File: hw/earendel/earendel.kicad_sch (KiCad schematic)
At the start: 0 parts

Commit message: Add LED ring drivers
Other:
- added sheet Inner Ring (inner_ring.kicad_sch)
- added sheet MCU (mcu.kicad_sch)
- added sheet Outer Ring (outer_ring.kicad_sch)
- added sheet Power (power.kicad_sch)
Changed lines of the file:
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@@
 		(company "Aaron & Ryan Shappell")
+	)
+	(sheet
+		(at 132.08 109.22)
+		(size 26.67 13.97)
+		(fields_autoplaced yes)
+		(stroke
+			(width 0.1524)
+			(type solid)
+		)
+		(fill
+			(color 0 0 0 0.0000)
+		)
+		(property "Sheetname" "Outer Ring"
+			(at 132.08 108.5084 0)
+			(effects
+				(font
+					(size 1.27 1.27)
+				)
+				(justify left bottom)
+			)
+		)
+		(property "Sheetfile" "outer_ring.kicad_sch"
+			(at 132.08 123.7746 0)
+			(effects
+				(font
+					(size 1.27 1.27)
+				)
+				(justify left top)
+			)
+		)
+		(instances
+			(project "earendel"
+				(path "/9f298bf9-d1b7-4300-ae61-070881d679f0"
+					(page "5")
+				)
+			)
+		)
+	)
+	(sheet
+		(at 81.28 58.42)
+		(size 20.32 16.51)
+		(fields_autoplaced yes)
+		(stroke
+			(width 0.1524)
+			(type solid)
+		)
+		(fill
+			(color 0 0 0 0.0000)
+		)
+		(property "Sheetname" "MCU"
+			(at 81.28 57.7084 0)
+			(effects
+				(font
+					(size 1.27 1.27)
+				)
+				(justify left bottom)
+			)
+		)
+		(property "Sheetfile" "mcu.kicad_sch"
+			(at 81.28 75.5146 0)
+			(effects
+				(font
+					(size 1.27 1.27)
+				)
+				(justify left top)
+			)
+		)
+		(instances
+			(project "earendel"
+				(path "/9f298bf9-d1b7-4300-ae61-070881d679f0"
+					(page "2")
+				)
+			)
+		)
+	)
+	(sheet
+		(at 78.74 110.49)
+		(size 25.4 13.97)
+		(fields_autoplaced yes)
+		(stroke
+			(width 0.1524)
+			(type solid)
+		)
+		(fill
+			(color 0 0 0 0.0000)
+		)
+		(property "Sheetname" "Inner Ring"
+			(at 78.74 109.7784 0)
+			(effects
+				(font
+					(size 1.27 1.27)
+				)
+				(justify left bottom)
+			)
+		)
+		(property "Sheetfile" "inner_ring.kicad_sch"
+			(at 78.74 125.0446 0)
+			(effects
+				(font
+					(size 1.27 1.27)
+				)
+				(justify left top)
+			)
+		)
+		(instances
+			(project "earendel"
+				(path "/9f298bf9-d1b7-4300-ae61-070881d679f0"
+					(page "4")
+				)
+			)
+		)
+	)
+	(sheet
+		(at 129.54 58.42)
+		(size 25.4 15.24)
+		(fields_autoplaced yes)
+		(stroke
+			(width 0.1524)
+			(type solid)
+		)
+		(fill
+			(color 0 0 0 0.0000)
+		)
+		(property "Sheetname" "Power"
+			(at 129.54 57.7084 0)
+			(effects
+				(font
+					(size 1.27 1.27)
+				)
+				(justify left bottom)
+			)
+		)
+		(property "Sheetfile" "power.kicad_sch"
+			(at 129.54 74.2446 0)
+			(effects
+				(font
+					(size 1.27 1.27)
+				)
+				(justify left top)
+			)
+		)
+		(instances
+			(project "earendel"
+				(path "/9f298bf9-d1b7-4300-ae61-070881d679f0"
+					(page "3")
+				)
+			)
+		)
 	)
 	(sheet_instances

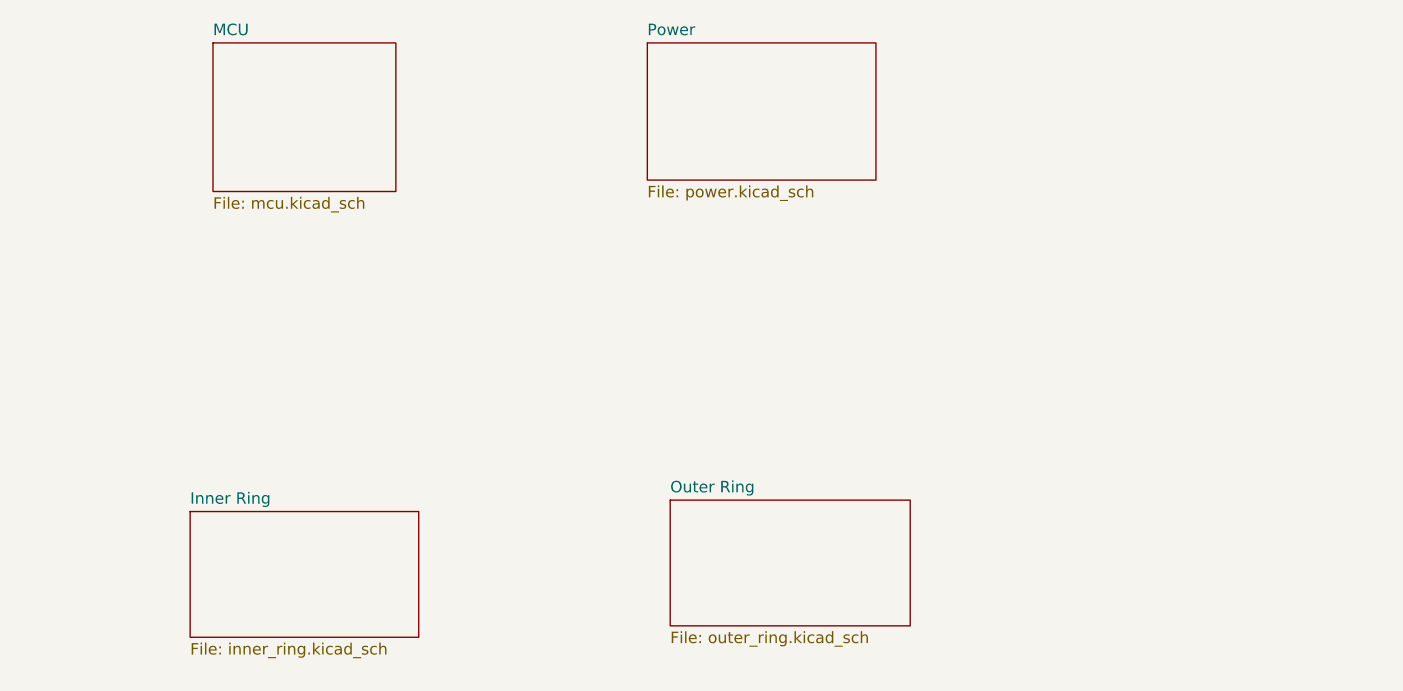
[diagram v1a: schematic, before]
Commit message: Added MCU decoupling caps, started power
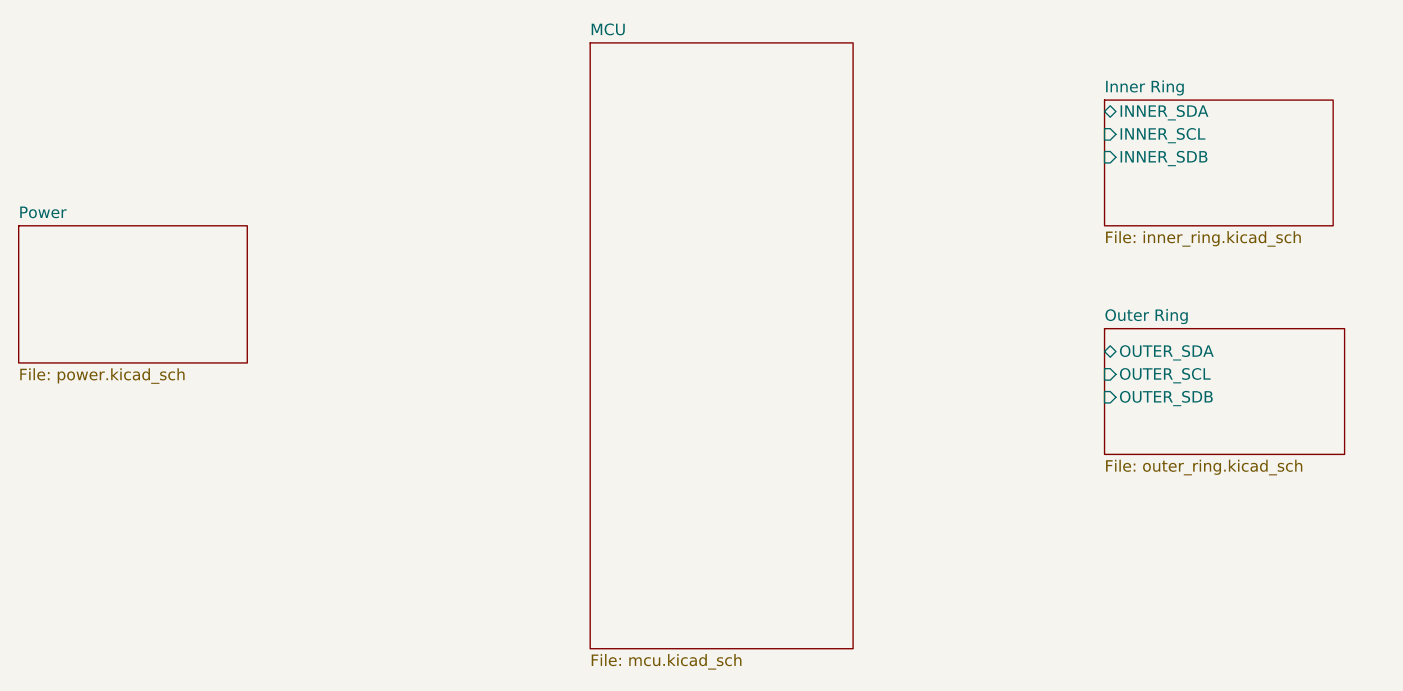
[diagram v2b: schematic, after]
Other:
- sheet Inner Ring ports: added INNER_SCL, INNER_SDA, INNER_SDB; removed none
- sheet Outer Ring ports: added OUTER_SCL, OUTER_SDA, OUTER_SDB; removed none
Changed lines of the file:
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@@
 	)
 	(sheet
-		(at 132.08 109.22)
+		(at 180.34 90.17)
 		(size 26.67 13.97)
 		(fields_autoplaced yes)
@@
 		)
 		(property "Sheetname" "Outer Ring"
-			(at 132.08 108.5084 0)
+			(at 180.34 89.4584 0)
 			(effects
 				(font
@@
 		)
 		(property "Sheetfile" "outer_ring.kicad_sch"
-			(at 132.08 123.7746 0)
+			(at 180.34 104.7246 0)
 			(effects
 				(font
@@
 				)
 				(justify left top)
+			)
+		)
+		(pin "OUTER_SDA" bidirectional
+			(at 180.34 92.71 180)
+			(effects
+				(font
+					(size 1.27 1.27)
+				)
+				(justify left)
+			)
+		)
+		(pin "OUTER_SCL" input
+			(at 180.34 95.25 180)
+			(effects
+				(font
+					(size 1.27 1.27)
+				)
+				(justify left)
+			)
+		)
+		(pin "OUTER_SDB" input
+			(at 180.34 97.79 180)
+			(effects
+				(font
+					(size 1.27 1.27)
+				)
+				(justify left)
 			)
 		)
@@
 	)
 	(sheet
-		(at 81.28 58.42)
-		(size 20.32 16.51)
+		(at 123.19 58.42)
+		(size 29.21 67.31)
 		(fields_autoplaced yes)
 		(stroke
@@
 		)
 		(property "Sheetname" "MCU"
-			(at 81.28 57.7084 0)
+			(at 123.19 57.7084 0)
 			(effects
 				(font
@@
 		)
 		(property "Sheetfile" "mcu.kicad_sch"
-			(at 81.28 75.5146 0)
+			(at 123.19 126.3146 0)
 			(effects
 				(font
@@
 	)
 	(sheet
-		(at 78.74 110.49)
+		(at 180.34 64.77)
 		(size 25.4 13.97)
 		(fields_autoplaced yes)
@@
 		)
 		(property "Sheetname" "Inner Ring"
-			(at 78.74 109.7784 0)
+			(at 180.34 64.0584 0)
 			(effects
 				(font
@@
 		)
 		(property "Sheetfile" "inner_ring.kicad_sch"
-			(at 78.74 125.0446 0)
+			(at 180.34 79.3246 0)
 			(effects
 				(font
@@
 				)
 				(justify left top)
+			)
+		)
+		(pin "INNER_SCL" input
+			(at 180.34 68.58 180)
+			(effects
+				(font
+					(size 1.27 1.27)
+				)
+				(justify left)
+			)
+		)
+		(pin "INNER_SDB" input
+			(at 180.34 71.12 180)
+			(effects
+				(font
+					(size 1.27 1.27)
+				)
+				(justify left)
+			)
+		)
+		(pin "INNER_SDA" bidirectional
+			(at 180.34 66.04 180)
+			(effects
+				(font
+					(size 1.27 1.27)
+				)
+				(justify left)
 			)
 		)
@@
 	)
 	(sheet
-		(at 129.54 58.42)
+		(at 59.69 78.74)
 		(size 25.4 15.24)
 		(fields_autoplaced yes)
@@
 		)
 		(property "Sheetname" "Power"
-			(at 129.54 57.7084 0)
+			(at 59.69 78.0284 0)
 			(effects
 				(font
@@
 		)
 		(property "Sheetfile" "power.kicad_sch"
-			(at 129.54 74.2446 0)
+			(at 59.69 94.5646 0)
 			(effects
 				(font
